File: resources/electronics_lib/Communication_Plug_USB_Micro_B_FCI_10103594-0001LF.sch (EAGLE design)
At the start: 5 parts, among them CN2 USB-RECEPTABLE

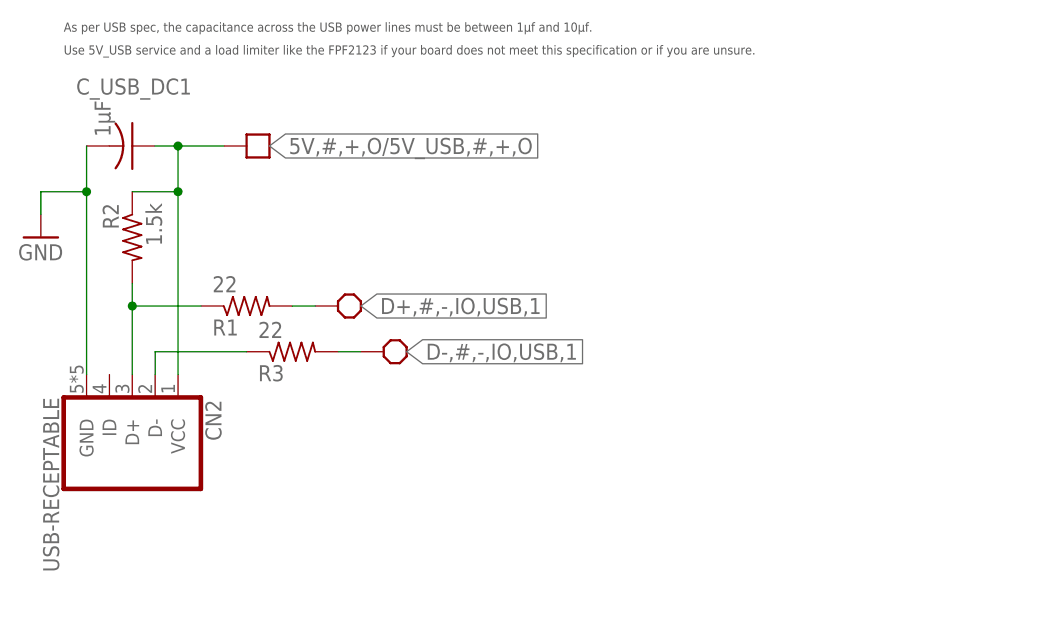
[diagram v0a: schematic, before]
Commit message: Changed schematics to pick an assigned service.
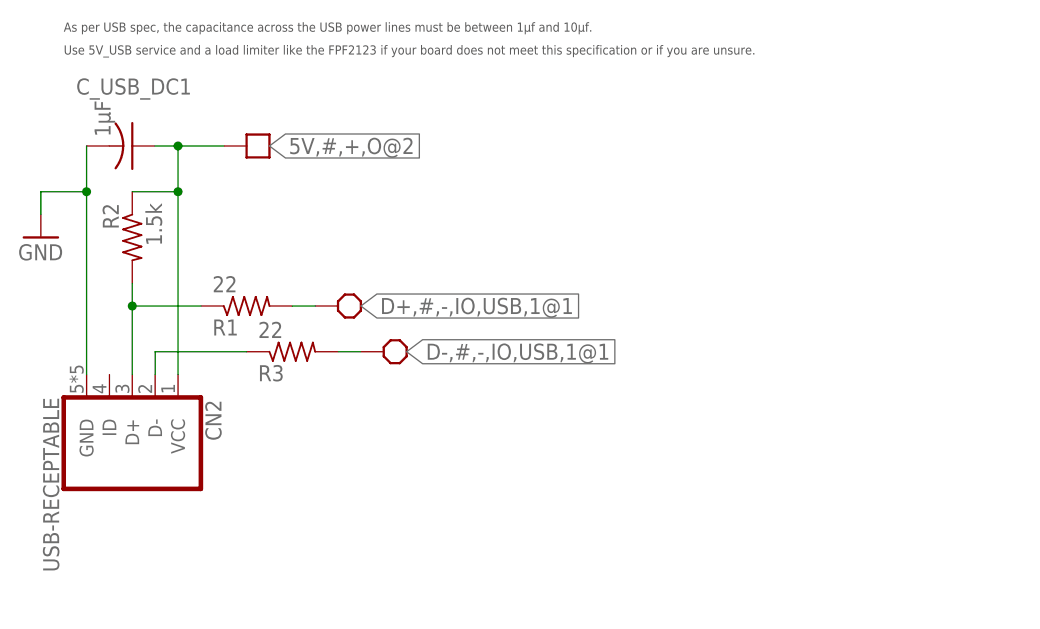
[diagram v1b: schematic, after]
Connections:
- net 5V,#,+,O/5V_USB,#,+,O renamed 5V,#,+,O@2
- net D+,#,-,IO,USB,1 renamed D+,#,-,IO,USB,1@1
- net D-,#,-,IO,USB,1 renamed D-,#,-,IO,USB,1@1
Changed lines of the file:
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@@
 </busses>
 <nets>
-<net name="5V,#,+,O/5V_USB,#,+,O" class="0">
+<net name="5V,#,+,O@2" class="0">
 <segment>
 <pinref part="C_USB_DC1" gate="G$1" pin="1"/>
@@
 </segment>
 </net>
-<net name="D+,#,-,IO,USB,1" class="0">
+<net name="D+,#,-,IO,USB,1@1" class="0">
 <segment>
 <pinref part="R1" gate="G$1" pin="2"/>
@@
 </segment>
 </net>
-<net name="D-,#,-,IO,USB,1" class="0">
+<net name="D-,#,-,IO,USB,1@1" class="0">
 <segment>
 <pinref part="R3" gate="G$1" pin="2"/>
